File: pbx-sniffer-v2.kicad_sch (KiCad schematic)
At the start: 1 part

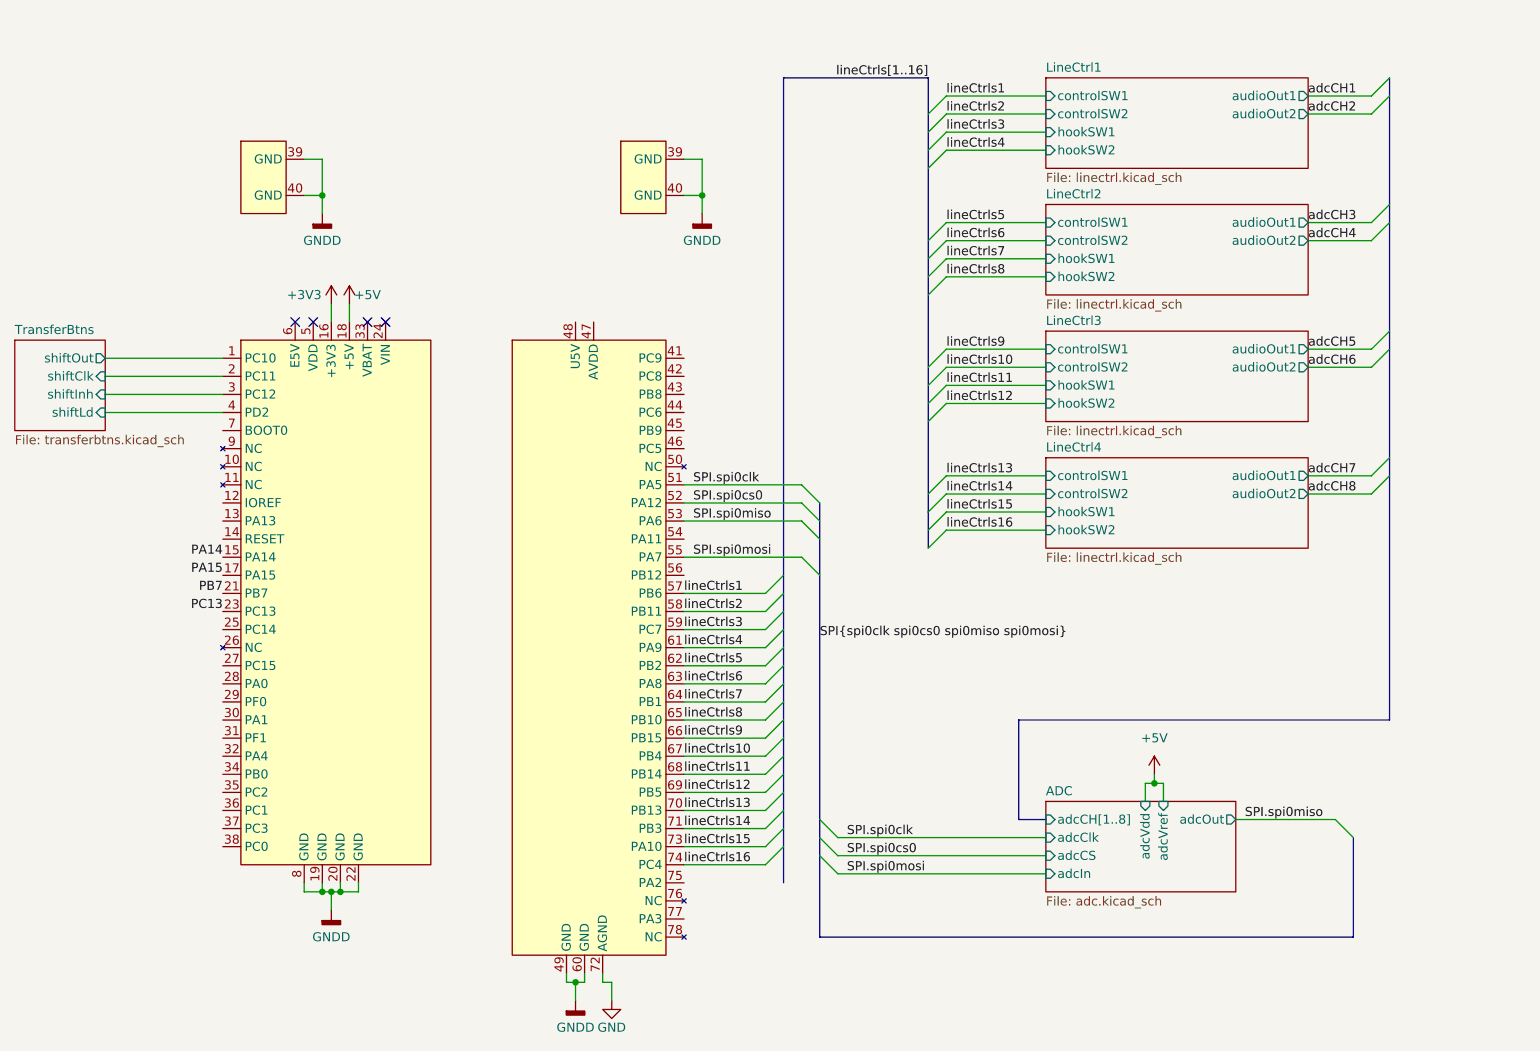
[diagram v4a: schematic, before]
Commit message: add test points throughout the schematic
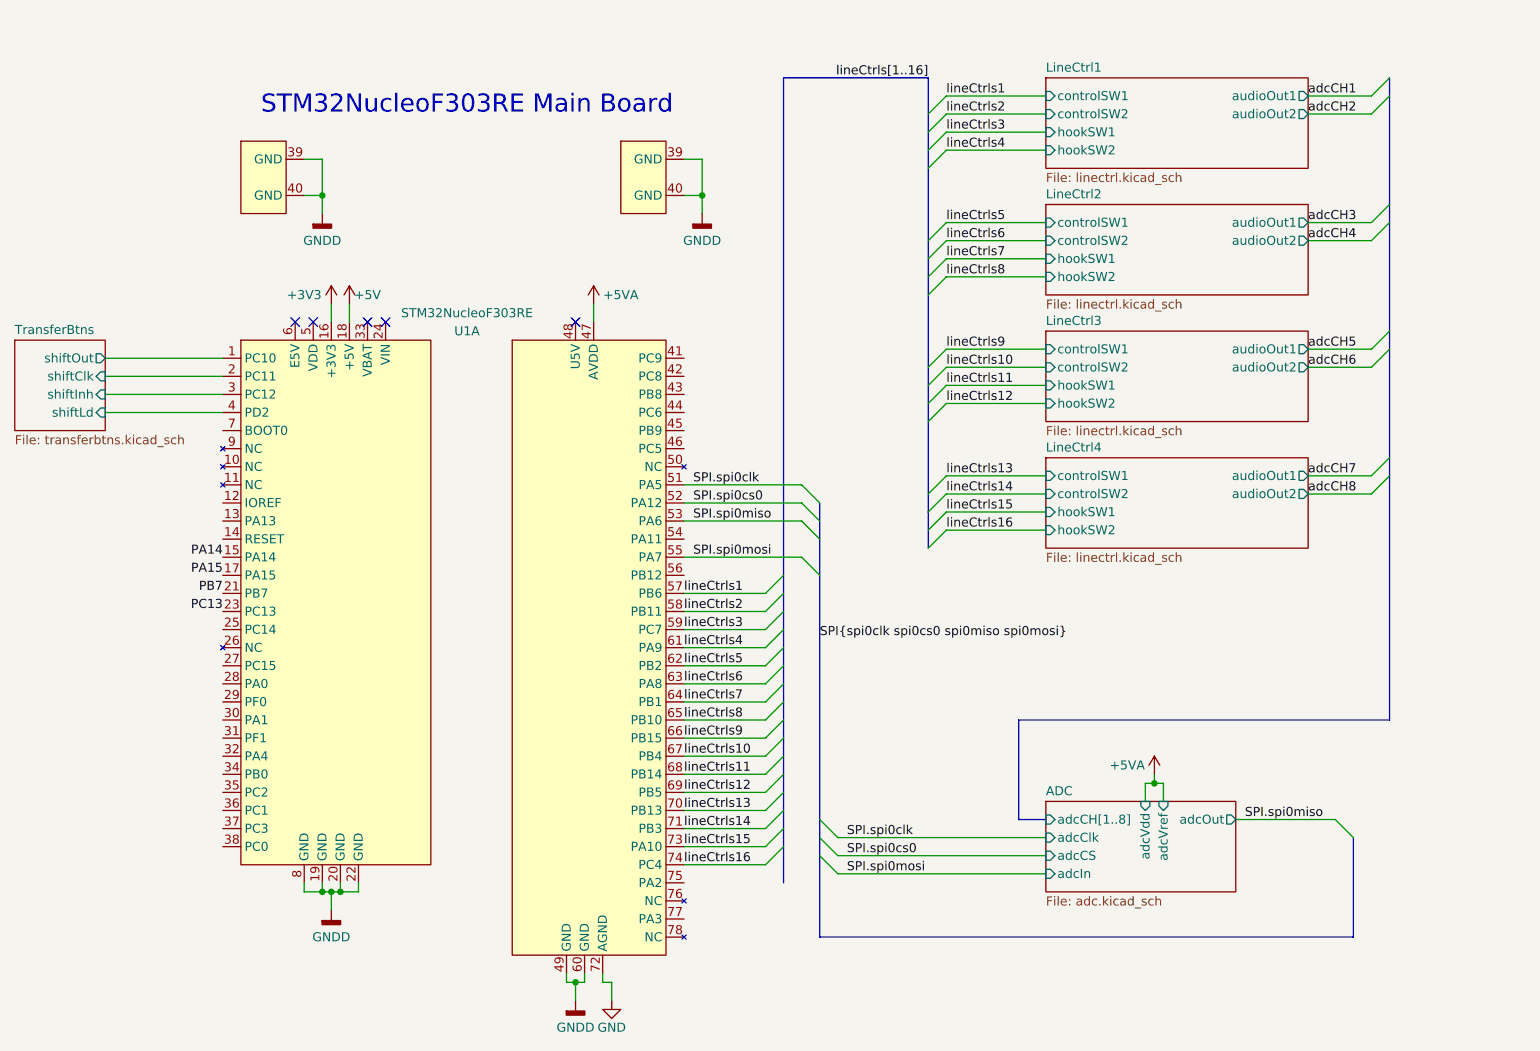
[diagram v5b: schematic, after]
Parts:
- U1: value (none) -> STM32NucleoF303RE; footprint (none) -> Nucleo:STM32NucleoF303RE
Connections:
- net +5VA: now reaches U1.47 (AVDD)
- no-connect marks 4 -> 5
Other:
- note added: "STM32NucleoF303RE Main Board"

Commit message: finish initial schematic design, start pcb layout
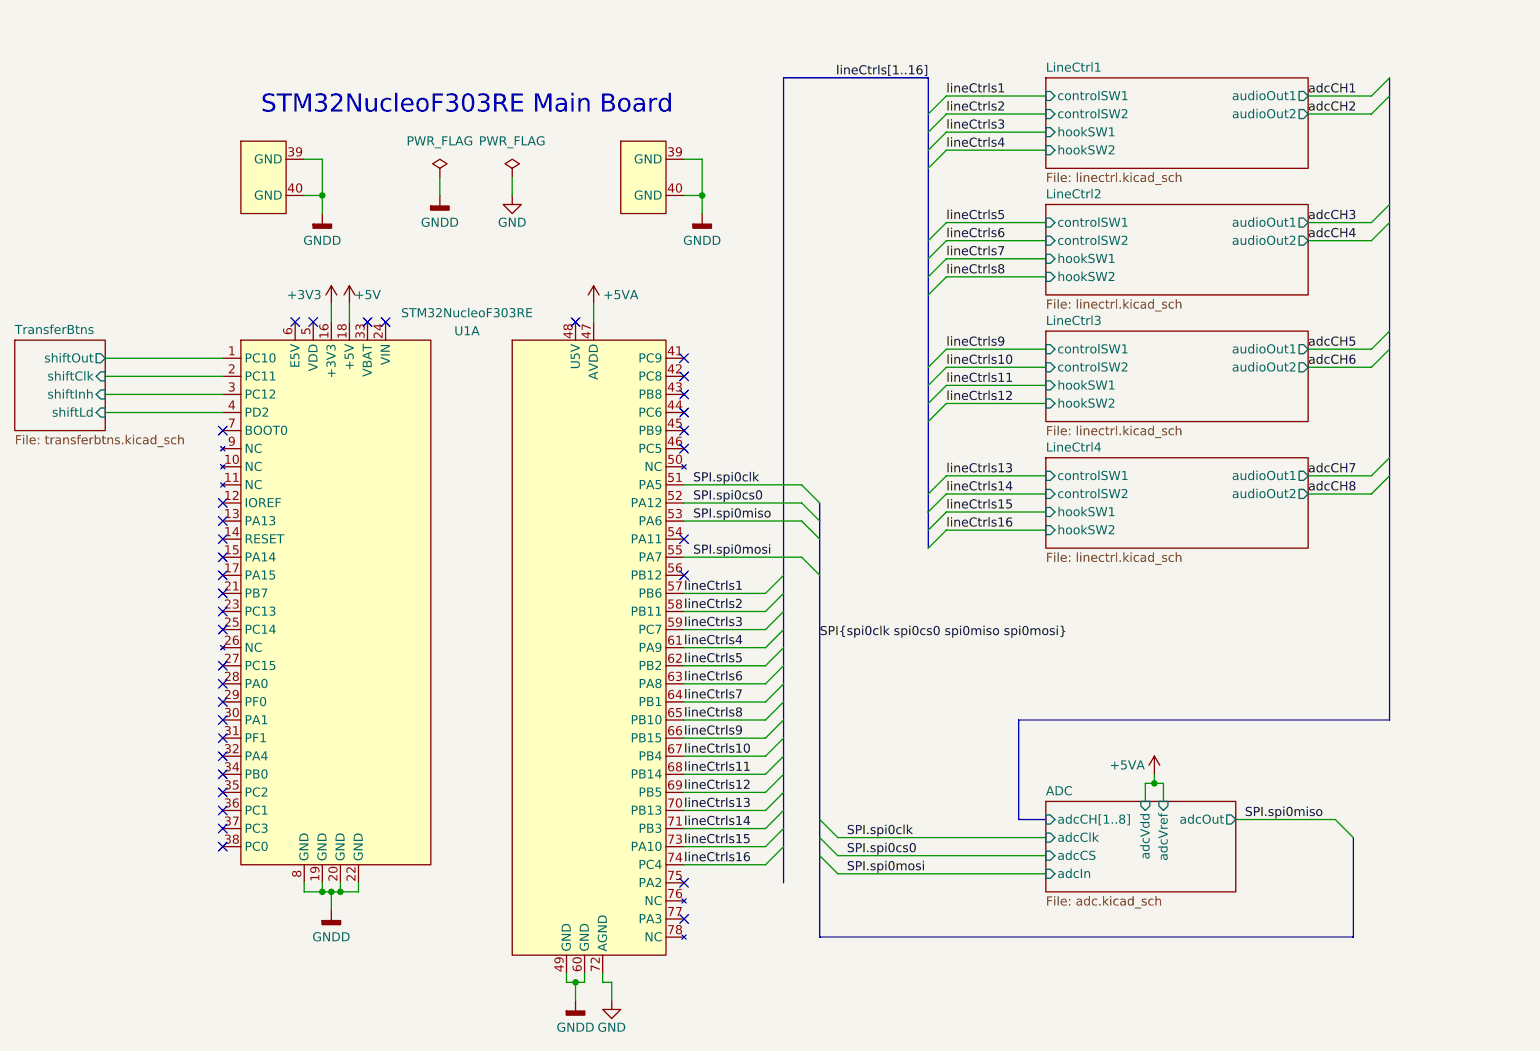
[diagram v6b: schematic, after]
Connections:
- net PA14: no longer names the net of U1.15 (PA14)
- net PA15: no longer names the net of U1.17 (PA15)
- net PB7: no longer names the net of U1.21 (PB7)
- net PC13: no longer names the net of U1.23 (PC13)
- no-connect marks 5 -> 35
